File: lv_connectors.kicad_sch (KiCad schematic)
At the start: 37 parts, among them J10 Conn_01x10, J11 Conn_01x04, J12 Conn_01x04, J15 Conn_01x10, J2 Conn_01x04, J3 Conn_01x04, J4 Conn_01x04, J5 Conn_01x02, J6 Conn_01x02, J7 Conn_01x02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

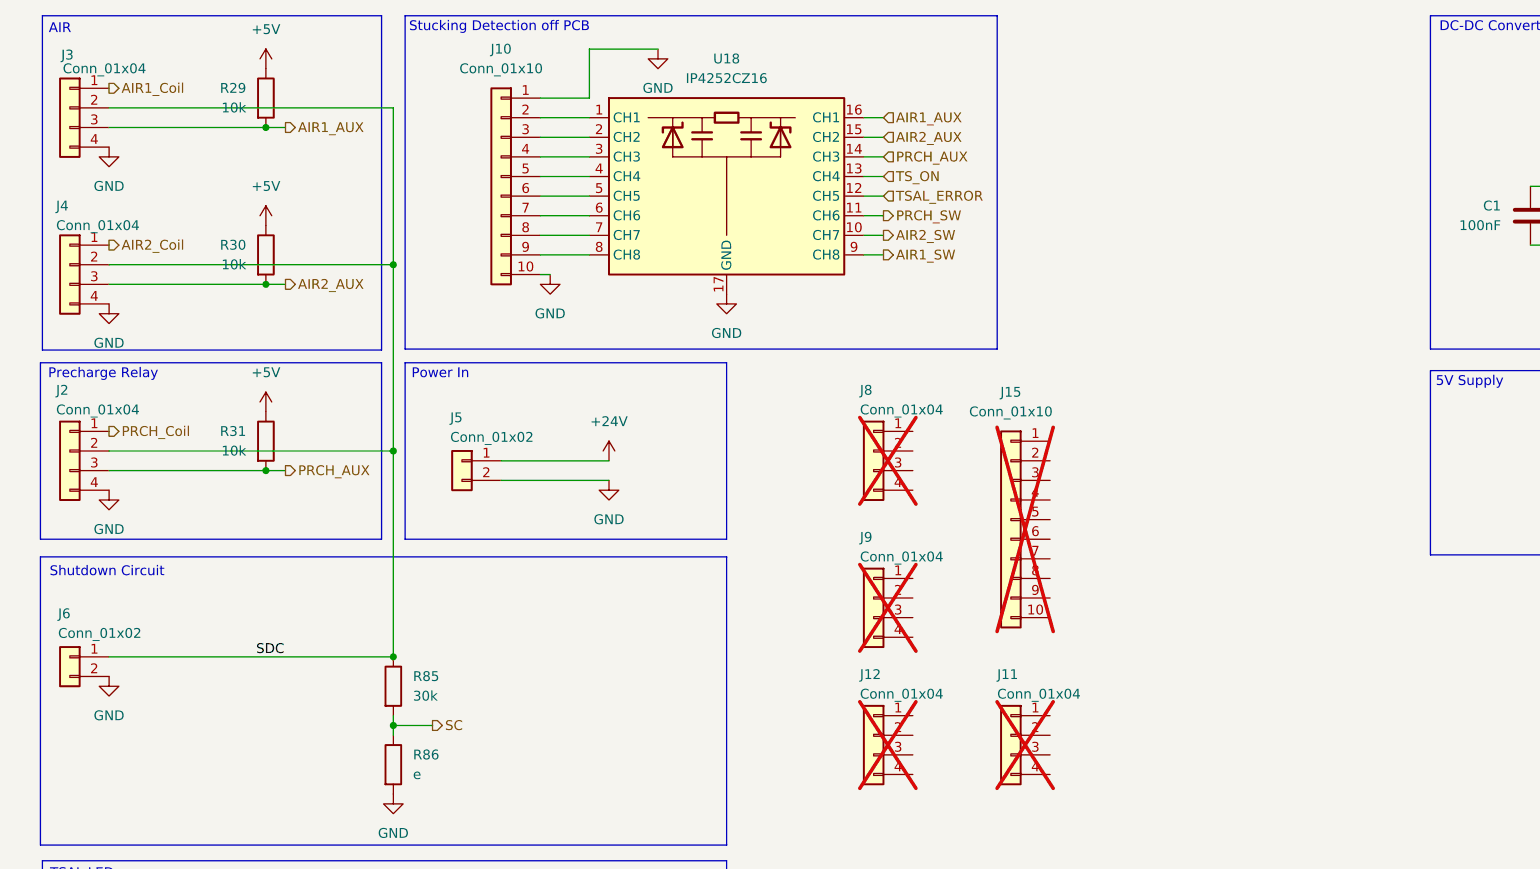
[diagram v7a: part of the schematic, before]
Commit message: Added TSAC Indicator with PSU
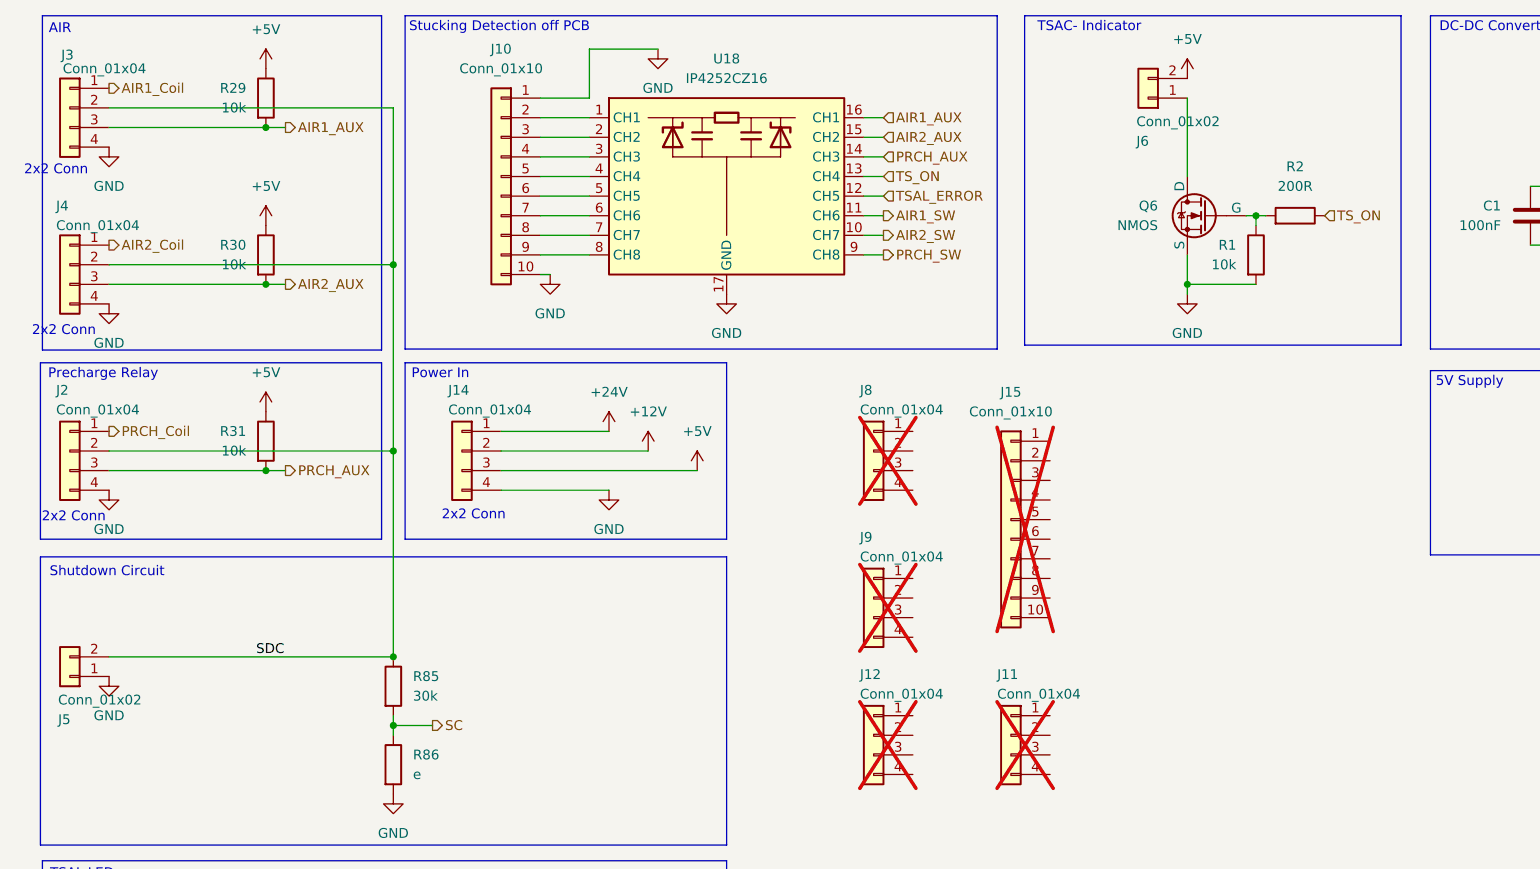
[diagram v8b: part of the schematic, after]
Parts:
- added J14: Conn_01x04, wuerth_conn:66200421022, symbol Connector_Generic:Conn_01x04
- added Q6: NMOS, Package_TO_SOT_SMD:SOT-23-3, symbol Simulation_SPICE:NMOS
- added R1: 10k, Resistor_SMD:R_0603_1608Metric, symbol Device:R
- added R2: 200R, Resistor_SMD:R_0603_1608Metric, symbol Device:R
- J6: footprint Connector_AMASS:AMASS_XT60-F_1x02_P7.20mm_Vertical -> Connector_JST:JST_XH_B2B-XH-A_1x02_P2.50mm_Vertical
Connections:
- net +24V: now also J14.1 (Pin_1); no longer J5.1 (Pin_1)
- net +5V: now also J6.2 (Pin_2), J14.3 (Pin_3)
- net AIR1_SW: now also U18.11 (CH6); no longer U18.9 (CH8)
- net GND: now also J5.1 (Pin_1), J14.4 (Pin_4), Q6.3 (S), R1.2; no longer J5.2 (Pin_2), J6.2 (Pin_2)
- net PRCH_SW: now also U18.9 (CH8); no longer U18.11 (CH6)
- net SDC: now also J5.2 (Pin_2); no longer J6.1 (Pin_1)
- net TS_ON: now also R2.1
- new net: Q6.2 (G), R1.1, R2.2
- new net: J6.1 (Pin_1), Q6.1 (D)
- new net +12V: J14.2 (Pin_2)
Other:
- note added: "2x2 Conn"
- note added: "TSAC- Indicator"
